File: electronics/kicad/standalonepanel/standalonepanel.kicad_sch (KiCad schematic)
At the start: 3 parts, among them U1 ESP32-WROOM-E, U2 ICE40HX4K-TQ144, U4 IS64WV25616EFBLL-10TLI

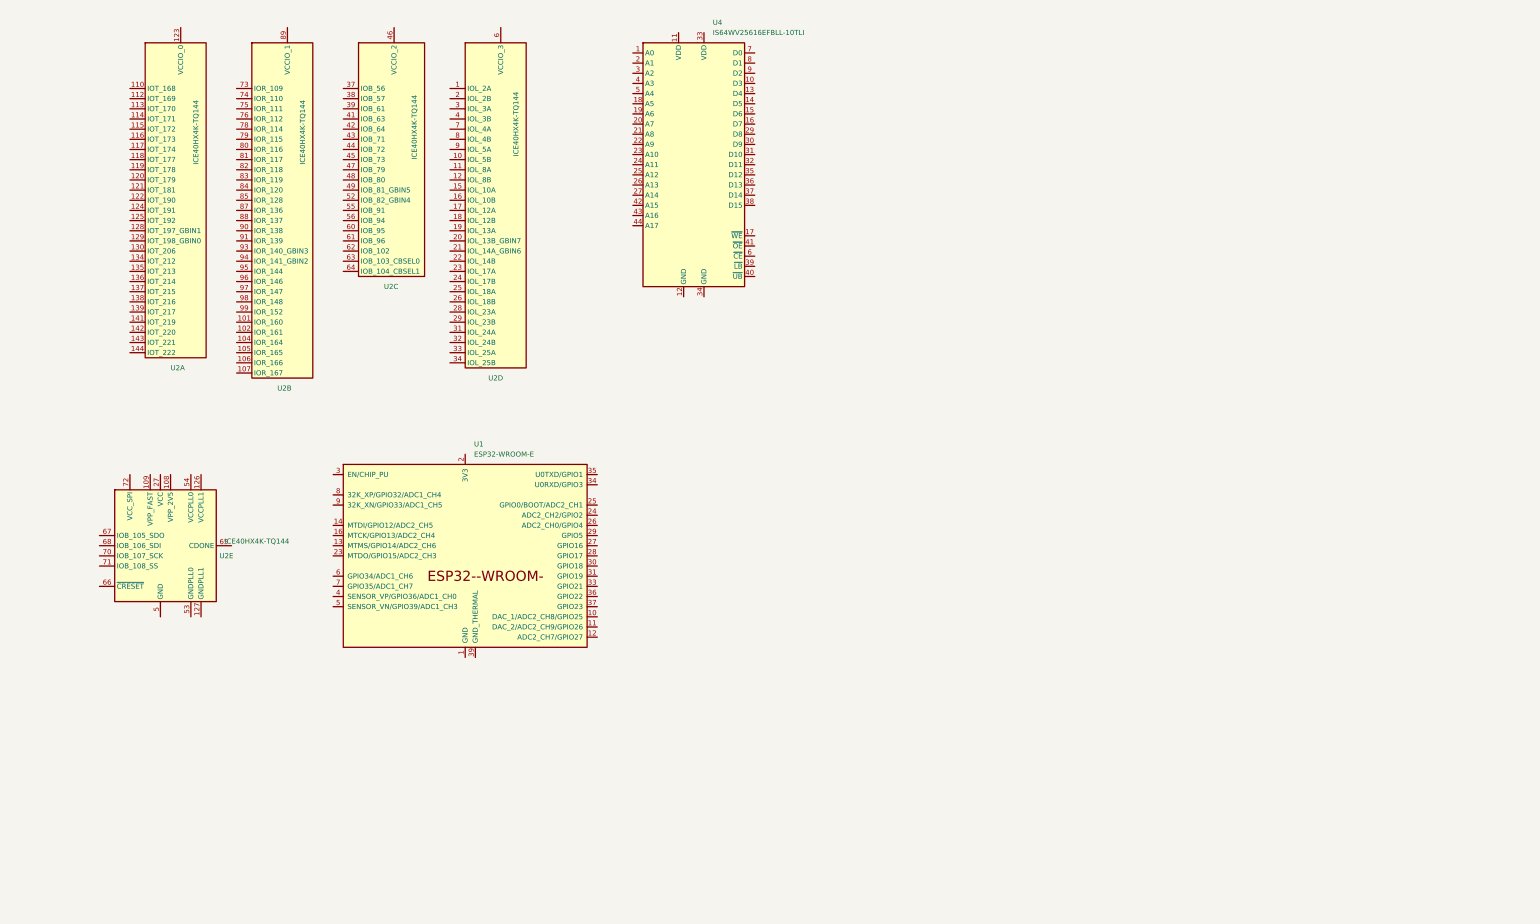
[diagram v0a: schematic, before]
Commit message: 3D Models v23 all ok, not tested with PCB All electronics designed including PCB - untested
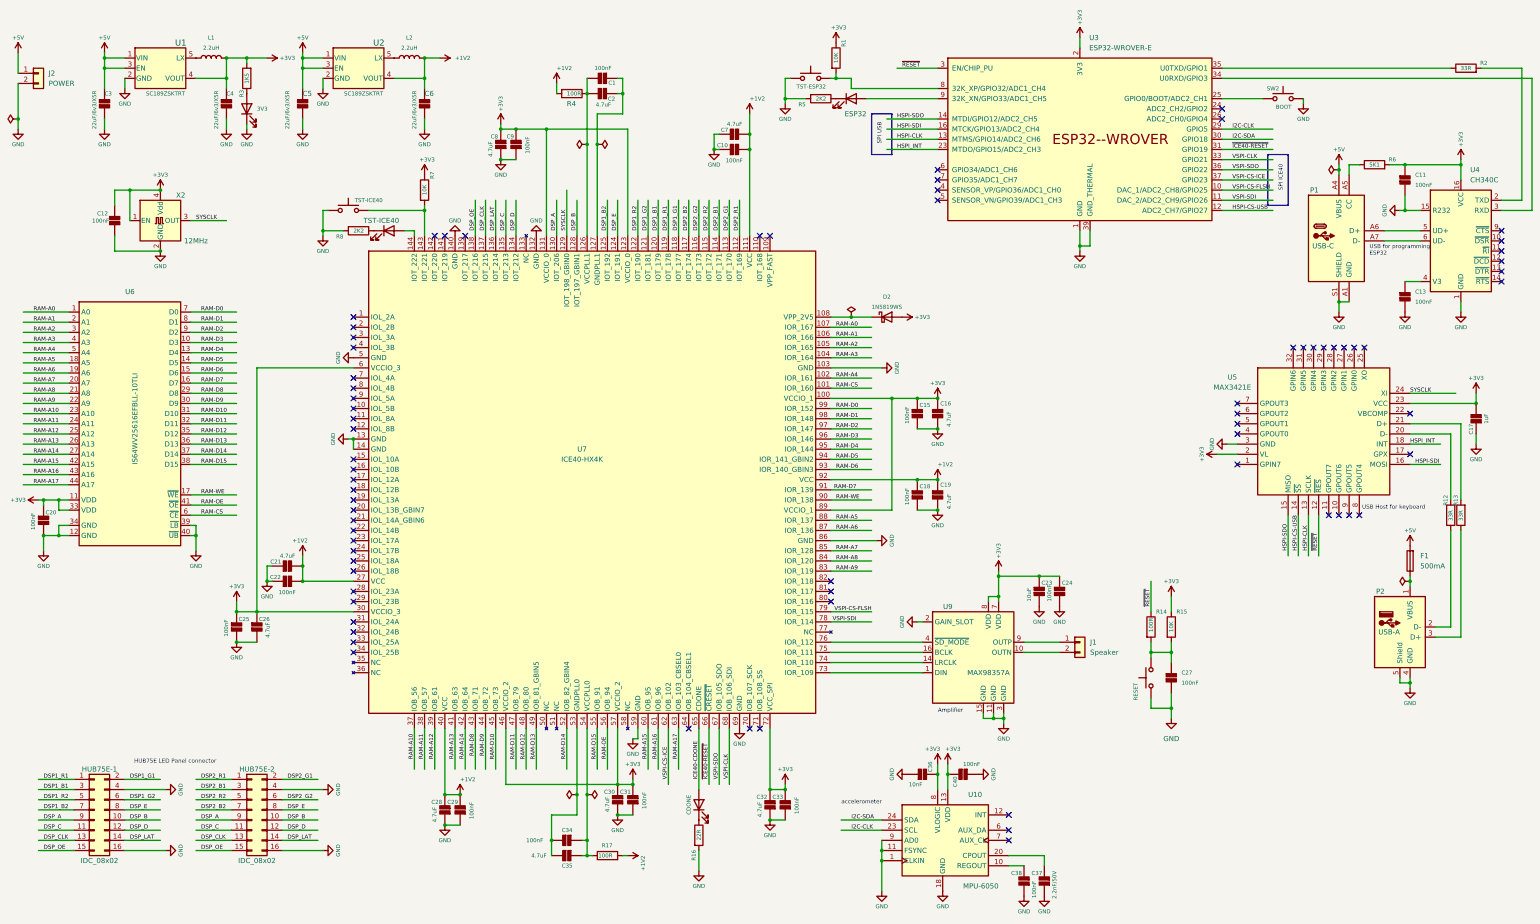
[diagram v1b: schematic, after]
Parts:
- removed U1: ESP32-WROOM-E, PCM_Espressif:ESP32-WROOM-32E, symbol PCM_Espressif:ESP32-WROOM-E
- removed U2: ICE40HX4K-TQ144, Package_QFP:TQFP-144_20x20mm_P0.5mm, symbol FPGA_Lattice:ICE40HX4K-TQ144
- removed U4: IS64WV25616EFBLL-10TLI, Package_SO:TSOP-II-44_10.16x18.41mm_P0.8mm, symbol 0_project:IS64WV25616EFBLL
- added C1, C10, C11, C12, C13, C15, C18, C20, C22, C24, C25, C27, C29, C31, C33, C34, C38, C40, C9: 100nF, Capacitor_SMD:C_0805_2012Metric_Pad1.18x1.45mm_HandSolder, symbol 0_project:C
- added C16, C19, C2, C21, C26, C28, C30, C32, C35, C7, C8: 4.7uF, Capacitor_SMD:C_0805_2012Metric_Pad1.18x1.45mm_HandSolder, symbol 0_project:C
- added C17: 1uF, Capacitor_SMD:C_0805_2012Metric_Pad1.18x1.45mm_HandSolder, symbol 0_project:C
- added C23: 10uF, Capacitor_SMD:C_0805_2012Metric_Pad1.18x1.45mm_HandSolder, symbol 0_project:C
- added C3, C4, C5, C6: 22uF/6v3/X5R, Capacitor_SMD:C_0805_2012Metric_Pad1.18x1.45mm_HandSolder, symbol 0_project:C
- added C36: 10nF, Capacitor_SMD:C_0805_2012Metric_Pad1.18x1.45mm_HandSolder, symbol 0_project:C
- added C37: 2.2nF/50V, Capacitor_SMD:C_0805_2012Metric_Pad1.18x1.45mm_HandSolder, symbol 0_project:C
- added D2: 1N5819WS, Diode_SMD:D_SOD-323, symbol Diode:1N5819WS
- added F1: 500mA, 0_project:FUSEHOLDER 1808, symbol 0_project:Fuse
- added HUB75E-1, HUB75E-2: IDC_08x02, 0_project:IDC-Header_2x08_P2.54mm_Horizontal, symbol Connector_Generic:Conn_02x08_Odd_Even
- added J1: Speaker, Connector_JST:JST_XH_S2B-XH-A_1x02_P2.50mm_Horizontal, symbol Connector_Generic:Conn_01x02
- added J2: POWER, Connector_JST:JST_XH_S2B-XH-A_1x02_P2.50mm_Horizontal, symbol Connector_Generic:Conn_01x02
- added L1, L2: 2.2uH, 0_project:Inductor-040420, symbol Device:L
- added LED1: ESP32, LED_SMD:LED_1206_3216Metric_Pad1.42x1.75mm_HandSolder, symbol Device:LED
- added LED2: 3V3, LED_SMD:LED_1206_3216Metric_Pad1.42x1.75mm_HandSolder, symbol Device:LED
- added LED3: TST-ICE40, LED_SMD:LED_1206_3216Metric_Pad1.42x1.75mm_HandSolder, symbol Device:LED
- added LED4: CDONE, LED_SMD:LED_1206_3216Metric_Pad1.42x1.75mm_HandSolder, symbol Device:LED
- added P1: USB-C, 0_project:USB_C_Receptacle_G-Switch_GT-USB-7010ASV, symbol 0_project:USB_C
- added P2: USB-A, 0_project:USB-A TH Female, symbol 0_project:USB_A
- added R1, R15, R7: 10K, Resistor_SMD:R_1206_3216Metric_Pad1.30x1.75mm_HandSolder, symbol Device:R
- added R12, R13, R2: 33R, Resistor_SMD:R_1206_3216Metric_Pad1.30x1.75mm_HandSolder, symbol Device:R
- added R14, R17, R4: 100R, Resistor_SMD:R_1206_3216Metric_Pad1.30x1.75mm_HandSolder, symbol Device:R
- added R16: 22R, Resistor_SMD:R_1206_3216Metric_Pad1.30x1.75mm_HandSolder, symbol Device:R
- added R3: 1K5, Resistor_SMD:R_1206_3216Metric_Pad1.30x1.75mm_HandSolder, symbol Device:R
- added R5, R8: 2K2, Resistor_SMD:R_1206_3216Metric_Pad1.30x1.75mm_HandSolder, symbol Device:R
- added R6: 5K1, Resistor_SMD:R_1206_3216Metric_Pad1.30x1.75mm_HandSolder, symbol Device:R
- added SW1: TST-ESP32, Button_Switch_SMD:SW_SPST_FSMSM, symbol Switch:SW_Push
- added SW2: BOOT, Button_Switch_SMD:SW_SPST_FSMSM, symbol Switch:SW_Push
- added SW3: TST-ICE40, Button_Switch_SMD:SW_SPST_FSMSM, symbol Switch:SW_Push
- added SW4: RESET, Button_Switch_SMD:SW_SPST_FSMSM, symbol Switch:SW_Push
- added U1, U2: SC189ZSKTRT, 0_project:SOT23-5-SC189_SEM, symbol 0_project:SC189ZSKTRT
- added U10: MPU-6050, 0_project:InvenSense_QFN-24_4x4mm_P0.5mm, symbol 0_project:MPU-6050
- added U3: ESP32-WROVER-E, 0_project:ESP32-WROVER-E, symbol 0_project:ESP32-WROVER-E
- added U4: CH340C, Package_SO:SOIC-16_3.9x9.9mm_P1.27mm, symbol 0_project:CH340C
- added U5: MAX3421E, 0_project:PQFP-32_5x5mm_P0.5mm, symbol 0_project:MAX3421E
- added U6: IS64WV25616EFBLL-10TLI, Package_SO:TSOP-II-44_10.16x18.41mm_P0.8mm, symbol 0_project:IS64WV25616EFBLL
- added U7: ICE40-HX4K, Package_QFP:TQFP-144_20x20mm_P0.5mm, symbol 0_project:ICE40HX4K-TQ144
- added U9: MAX98357A, Package_DFN_QFN:TQFN-16-1EP_3x3mm_P0.5mm_EP1.6x1.6mm, symbol 0_project:MAX98357A
- added X2: 12MHz, 0_project:Oscillator_SMD_EuroQuartz_XO91-4Pin_7.0x5.0mm_HandSoldering, symbol 0_project:TXC-7C
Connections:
- new net: LED3.1 (K), R8.1
- new net: LED3.2 (A), U7.144 (IOT_222)
- new net: SW2.1, U3.25 (GPIO0/BOOT/ADC2_CH1)
- new net: U3.34 (U0RXD/GPIO3), U4.3 (RXD)
- new net: R2.1, U3.35 (U0TXD/GPIO1)
- new net: R1.2, SW1.2, U3.8 (32K_XP/GPIO32/ADC1_CH4)
- new net: LED1.2 (A), U3.9 (32K_XN/GPIO33/ADC1_CH5)
- new net: C1.1, C2.1, U7.127 (GNDPLL1)
- new net: C1.2, C2.2, R4.1, U7.126 (VCCPLL1)
- new net: LED4.1 (K), R16.1
- new net: LED2.2 (A), R3.1
- new net: R7.2, SW3.2, U7.143 (IOT_221)
- new net: D2.1 (K), U7.108 (VPP_2V5)
- new net: F1.1, P2.1 (VBUS)
- new net: P2.2 (D-), R12.1
- new net: P2.3 (D+), R13.1
- new net: R2.2, U4.2 (TXD)
- new net: C34.1, C35.1, R17.1, U7.54 (VCCPLL0)
- new net: L1.1, U1.5 (LX)
- new net: J1.1 (Pin_1), U9.9 (OUTP)
- new net: J1.2 (Pin_2), U9.10 (OUTN)
- new net: P1.A5 (CC), R6.1
- new net: P1.A6 (D+), U4.5 (UD+)
- new net: P1.A7 (D-), U4.6 (UD-)
- new net: R12.2, U5.20 (D-)
- new net: R13.2, U5.21 (D+)
- new net: C27.1, R14.2, R15.2, SW4.2
- new net: C13.1, U4.4 (V3)
- new net: C34.2, C35.2, U7.53 (GNDPLL0)
- new net: U7.73 (IOR_109), U9.1 (DIN)
- new net: U7.74 (IOR_110), U9.14 (LRCLK)
- new net: U7.75 (IOR_111), U9.16 (BCLK)
- new net: U7.76 (IOR_112), U9.4 (~{SD_MODE})
- new net: LED1.1 (K), R5.1
- new net: C38.2, U10.10 (REGOUT)
- new net: C37.2, U10.20 (CPOUT)
- new net: L2.1, U2.5 (LX)
- new net +1V2: C10.2, C18.1, C19.1, C21.2, C22.2, C28.2, C29.2, C6.1, C7.2, L2.2, R17.2, R4.2, U2.4 (VOUT), U7.111 (VCC), U7.27 (VCC), U7.40 (VCC), U7.92 (VCC)
- new net +3V3: C11.1, C12.1, C15.1, C16.1, C17.2, C20.1, C23.1, C24.1, C25.1, C26.1, C30.2, C31.2, C32.2, C33.2, C36.2, C4.1, C40.2, C8.2, C9.2, D2.2 (A), L1.2, R1.1, R15.1, R3.2, R6.2, R7.1, U1.4 (VOUT), U10.13 (VDD), U10.8 (VLOGIC), U3.2 (3V3), U4.16 (VCC), U5.2 (VL), U5.23 (VCC), U6.11 (VDD), U6.33 (VDD), U7.100 (VCCIO_1), U7.123 (VCCIO_0), U7.131 (VCCIO_0), U7.30 (VCCIO_3), U7.46 (VCCIO_2), U7.57 (VCCIO_2), U7.6 (VCCIO_3), U7.72 (VCC_SPI), U7.89 (VCCIO_1), U9.7 (VDD), U9.8 (VDD), X2.1 (EN), X2.4 (Vdd)
- new net +5V: C3.1, C5.1, F1.2, J2.1 (Pin_1), P1.A4 (VBUS), P1.A9 (VBUS), P1.B4 (VBUS), P1.B9 (VBUS), U1.1 (VIN), U1.3 (EN), U2.1 (VIN), U2.3 (EN)
- new net DSP1_B1: HUB75E-1.3 (Pin_3), U7.120 (IOT_179)
- new net DSP1_B2: HUB75E-1.7 (Pin_7), U7.125 (IOT_192)
- new net DSP1_G1: HUB75E-1.2 (Pin_2), U7.118 (IOT_177)
- new net DSP1_G2: HUB75E-1.6 (Pin_6), U7.121 (IOT_181)
- new net DSP1_R1: HUB75E-1.1 (Pin_1), U7.119 (IOT_178)
- new net DSP1_R2: HUB75E-1.5 (Pin_5), U7.122 (IOT_190)
- new net DSP2_B1: HUB75E-2.3 (Pin_3), U7.114 (IOT_171)
- new net DSP2_B2: HUB75E-2.7 (Pin_7), U7.117 (IOT_174)
- new net DSP2_G1: HUB75E-2.2 (Pin_2), U7.113 (IOT_170)
- new net DSP2_G2: HUB75E-2.6 (Pin_6), U7.116 (IOT_173)
- new net DSP2_R1: HUB75E-2.1 (Pin_1), U7.112 (IOT_169)
- new net DSP2_R2: HUB75E-2.5 (Pin_5), U7.115 (IOT_172)
- new net DSP_A: HUB75E-1.9 (Pin_9), HUB75E-2.9 (Pin_9), U7.130 (IOT_206)
- new net DSP_B: HUB75E-1.10 (Pin_10), HUB75E-2.10 (Pin_10), U7.128 (IOT_197_GBIN1)
- new net DSP_C: HUB75E-1.11 (Pin_11), HUB75E-2.11 (Pin_11), U7.135 (IOT_213)
- new net DSP_CLK: HUB75E-1.13 (Pin_13), HUB75E-2.13 (Pin_13), U7.137 (IOT_215)
- new net DSP_D: HUB75E-1.12 (Pin_12), HUB75E-2.12 (Pin_12), U7.134 (IOT_212)
- new net DSP_E: HUB75E-1.8 (Pin_8), HUB75E-2.8 (Pin_8), U7.124 (IOT_191)
- new net DSP_LAT: HUB75E-1.14 (Pin_14), HUB75E-2.14 (Pin_14), U7.136 (IOT_214)
- new net DSP_OE: HUB75E-1.15 (Pin_15), HUB75E-2.15 (Pin_15), U7.138 (IOT_216)
- new net GND: C10.1, C11.2, C12.2, C13.2, C15.2, C16.2, C17.1, C18.2, C19.2, C20.2, C21.1, C22.1, C23.2, C24.2, C25.2, C26.2, C27.2, C28.1, C29.1, C3.2, C30.1, C31.1, C32.1, C33.1, C36.1, C37.1, C38.1, C4.2, C40.1, C5.2, C6.2, C7.1, C8.1, C9.1, HUB75E-1.16 (Pin_16), HUB75E-1.4 (Pin_4), HUB75E-2.16 (Pin_16), HUB75E-2.4 (Pin_4), J2.2 (Pin_2), LED2.1 (K), P1.A1 (GND), P1.A12 (GND), P1.B1 (GND), P1.B12 (GND), P1.S1 (SHIELD), P2.4 (GND), P2.5 (Shield), R16.2, R5.2, R8.2, SW1.1, SW2.2, SW3.1, SW4.1, U1.2 (GND), U10.1 (CLKIN), U10.11 (FSYNC), U10.18 (GND), U10.9 (AD0), U2.2 (GND), U3.1 (GND), U3.15 (GND), U3.38 (GND), U3.39 (GND_THERMAL), U4.1 (GND), U4.15 (R232), U5.3 (GND), U6.12 (GND), U6.34 (GND), U6.39 (~{LB}), U6.40 (~{UB}), U7.103 (GND), U7.13 (GND), U7.132 (GND), U7.14 (GND), U7.140 (GND), U7.5 (GND), U7.59 (GND), U7.69 (GND), U7.86 (GND), U9.11 (GND), U9.15 (GND), U9.2 (GAIN_SLOT), U9.3 (GND), X2.2 (GND)
- new net HSPI-CLK: U3.13 (MTMS/GPIO14/ADC2_CH6), U5.13 (SCLK)
- new net HSPI-CS-USB: U3.12 (ADC2_CH7/GPIO27), U5.14 (~{SS})
- new net HSPI-SDI: U3.16 (MTCK/GPIO13/ADC2_CH4), U5.16 (MOSI)
- new net HSPI-SDO: U3.14 (MTDI/GPIO12/ADC2_CH5), U5.15 (MISO)
- new net HSPI_INT: U3.23 (MTDO/GPIO15/ADC2_CH3), U5.18 (INT)
- new net I2C-CLK: U10.23 (SCL), U3.29 (GPIO5)
- new net I2C-SDA: U10.24 (SDA), U3.30 (GPIO18)
- new net ICE40-CDONE: LED4.2 (A), U7.65 (CDONE)
- new net RAM-A0: U6.1 (A0), U7.107 (IOR_167)
- new net RAM-A1: U6.2 (A1), U7.106 (IOR_166)
- new net RAM-A10: U6.23 (A10), U7.37 (IOB_56)
- new net RAM-A11: U6.24 (A11), U7.38 (IOB_57)
- new net RAM-A12: U6.25 (A12), U7.39 (IOB_61)
- new net RAM-A13: U6.26 (A13), U7.41 (IOB_63)
- new net RAM-A14: U6.27 (A14), U7.42 (IOB_64)
- new net RAM-A15: U6.42 (A15), U7.60 (IOB_95)
- new net RAM-A16: U6.43 (A16), U7.61 (IOB_96)
- new net RAM-A17: U6.44 (A17), U7.63 (IOB_103_CBSEL0)
- new net RAM-A2: U6.3 (A2), U7.105 (IOR_165)
- new net RAM-A3: U6.4 (A3), U7.104 (IOR_164)
- new net RAM-A4: U6.5 (A4), U7.102 (IOR_161)
- new net RAM-A5: U6.18 (A5), U7.88 (IOR_137)
- new net RAM-A6: U6.19 (A6), U7.87 (IOR_136)
- new net RAM-A7: U6.20 (A7), U7.85 (IOR_128)
- new net RAM-A8: U6.21 (A8), U7.84 (IOR_120)
- new net RAM-A9: U6.22 (A9), U7.83 (IOR_119)
- new net RAM-CS: U6.6 (~{CE}), U7.101 (IOR_160)
- new net RAM-D0: U6.7 (D0), U7.99 (IOR_152)
- new net RAM-D1: U6.8 (D1), U7.98 (IOR_148)
- new net RAM-D10: U6.31 (D10), U7.45 (IOB_73)
- new net RAM-D11: U6.32 (D11), U7.47 (IOB_79)
- new net RAM-D12: U6.35 (D12), U7.48 (IOB_80)
- new net RAM-D13: U6.36 (D13), U7.49 (IOB_81_GBIN5)
- new net RAM-D14: U6.37 (D14), U7.52 (IOB_82_GBIN4)
- new net RAM-D15: U6.38 (D15), U7.55 (IOB_91)
- new net RAM-D2: U6.9 (D2), U7.97 (IOR_147)
- new net RAM-D3: U6.10 (D3), U7.96 (IOR_146)
- new net RAM-D4: U6.13 (D4), U7.95 (IOR_144)
- new net RAM-D5: U6.14 (D5), U7.94 (IOR_141_GBIN2)
- new net RAM-D6: U6.15 (D6), U7.93 (IOR_140_GBIN3)
- new net RAM-D7: U6.16 (D7), U7.91 (IOR_139)
- new net RAM-D8: U6.29 (D8), U7.43 (IOB_71)
- new net RAM-D9: U6.30 (D9), U7.44 (IOB_72)
- new net RAM-OE: U6.41 (~{OE}), U7.56 (IOB_94)
- new net RAM-WE: U6.17 (~{WE}), U7.90 (IOR_138)
- new net SYSCLK: U5.24 (XI), U7.129 (IOT_198_GBIN0), X2.3 (OUT)
- new net VSPI-CLK: U3.33 (GPIO21), U7.68 (IOB_106_SDI)
- new net VSPI-CS-FLSH: U3.10 (DAC_1/ADC2_CH8/GPIO25), U7.79 (IOR_115)
- new net VSPI-CS-ICE: U3.37 (GPIO23), U7.62 (IOB_102)
- new net VSPI-SDI: U3.11 (DAC_2/ADC2_CH9/GPIO26), U7.78 (IOR_114)
- new net VSPI-SDO: U3.36 (GPIO22), U7.67 (IOB_105_SDO)
- new net ~{ICE40-RESET}: U3.31 (GPIO19), U7.66 (~{CRESET})
- new net ~{RESET}: R14.1, U3.3 (EN/CHIP_PU), U5.12 (~{RES})
- no-connect marks 0 -> 73
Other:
- note added: "Amplifier"
- note added: "HUB75E LED Panel connector"
- note added: "SPI ICE40"
- note added: "SPI USB"
- note added: "USB Host for keyboard"
- note added: "USB for programming ESP32"
- note added: "accelerometer"
